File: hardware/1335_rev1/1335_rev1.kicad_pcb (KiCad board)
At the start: 2 copper layers, 45 x 45 mm, 11 parts, among them J1 Screw_Terminal_01x05, J2 Screw_Terminal_01x05, U1 A1335

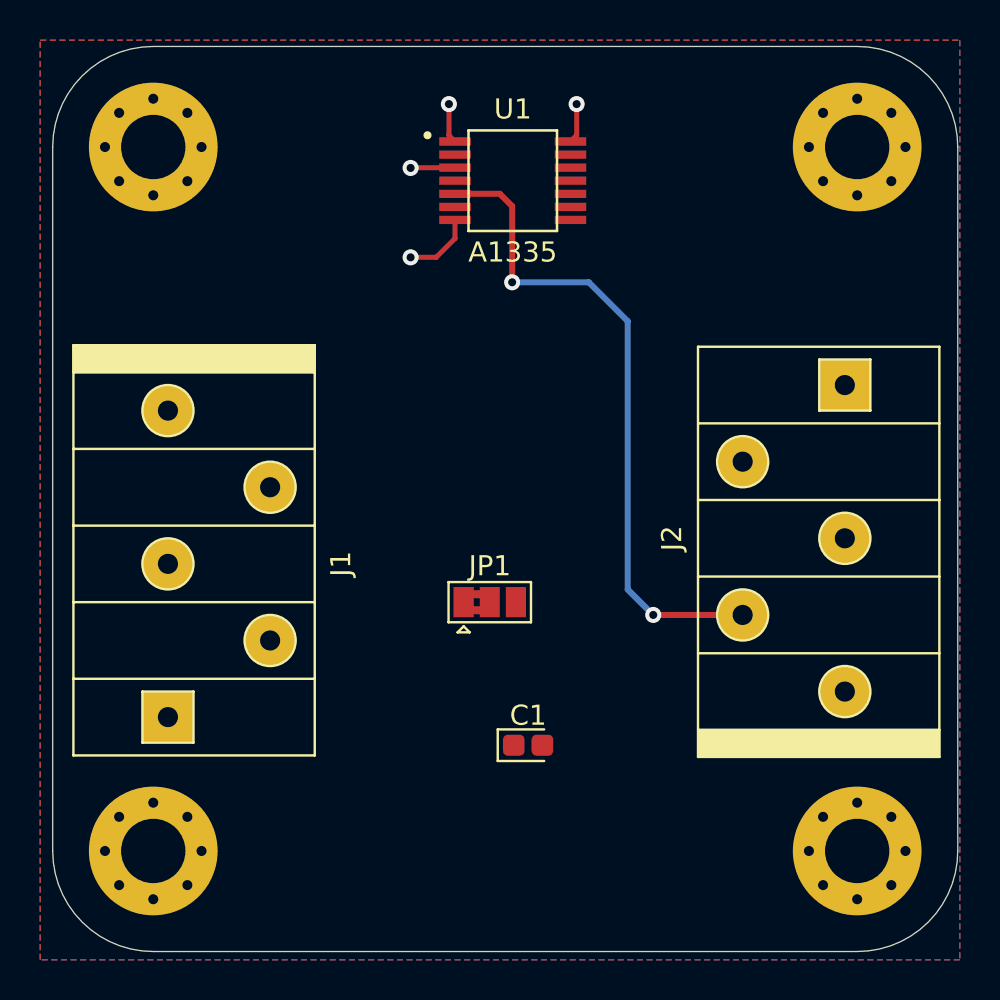
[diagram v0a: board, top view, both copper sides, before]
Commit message: Add 3d models, send to review pcb
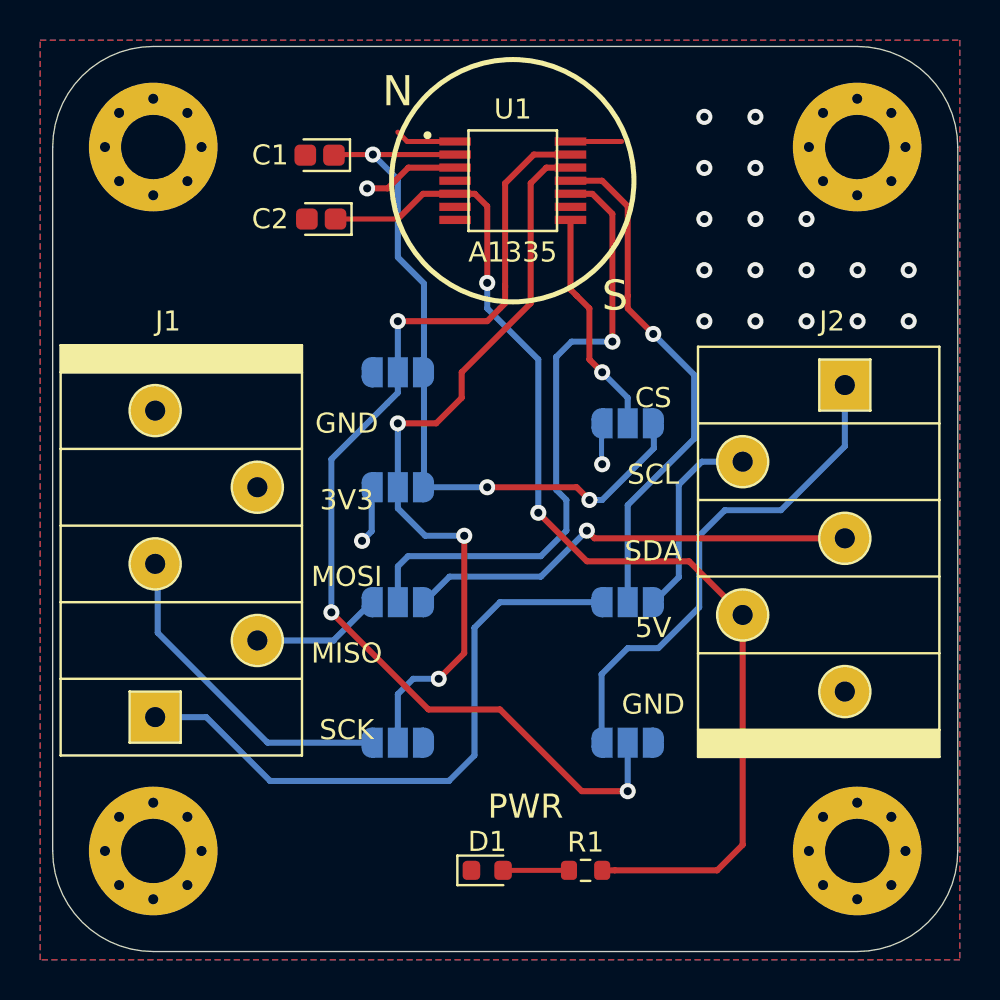
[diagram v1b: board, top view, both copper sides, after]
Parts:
- removed REF**: KiCad-Logo2_6mm_SilkScreen, Symbol:KiCad-Logo2_6mm_SilkScreen
- added C2: 100n, Capacitor_Tantalum_SMD:CP_EIA-1608-08_AVX-J, F.Cu at (133.3, 68.6)
- added D1: LED, LED_SMD:LED_0603_1608Metric, F.Cu at (141.6, 101.0)
- added JP2: Jumper_NC_Dual, Jumper:SolderJumper-3_P1.3mm_Open_RoundedPad1.0x1.5mm_NumberLabels, B.Cu at (148.6, 87.6)
- added JP3: Jumper_NC_Dual, Jumper:SolderJumper-3_P1.3mm_Open_RoundedPad1.0x1.5mm_NumberLabels, B.Cu at (148.6, 94.6)
- added JP4: Jumper_NC_Dual, Jumper:SolderJumper-3_P1.3mm_Open_RoundedPad1.0x1.5mm_NumberLabels, B.Cu at (137.2, 76.2)
- added JP5: Jumper_NC_Dual, Jumper:SolderJumper-3_P1.3mm_Open_RoundedPad1.0x1.5mm_NumberLabels, B.Cu at (137.2, 87.6)
- added JP6: Jumper_NC_Dual, Jumper:SolderJumper-3_P1.3mm_Open_RoundedPad1.0x1.5mm_NumberLabels, B.Cu at (137.2, 94.6)
- added JP7: Jumper_NC_Dual, Jumper:SolderJumper-3_P1.3mm_Open_RoundedPad1.0x1.5mm_NumberLabels, B.Cu at (137.2, 81.9)
- added R1: 1k, Resistor_SMD:R_0603_1608Metric, F.Cu at (146.5, 101.0)
- C1: value CP1 -> 100n
- JP1: value Jumper_3_Bridged12 -> Jumper_NC_Dual; footprint Jumper:SolderJumper-3_P1.3mm_Bridged2Bar12_Pad1.0x1.5mm -> Jumper:SolderJumper-3_P1.3mm_Open_RoundedPad1.0x1.5mm_NumberLabels; moved to B.Cu
- moved C1 31.1 mm to (133.3, 65.4), turned to 180 degrees
- moved JP1 11.2 mm to (148.6, 78.7), turned to 180 degrees
- moved G*** 1.27 mm to (142.2, 101.6)
- moved J1 0.64 mm to (125.1, 85.7)
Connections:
- JP1 pad 1: GND -> /BYP
- JP1 pad 3: /BYP -> GND
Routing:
- net /SA0-CS: track 0.00 -> 52.3 mm, vias 0 -> 3
- net /SA1-MOSI: track 0.00 -> 38.6 mm, vias 0 -> 3
- net /BYP: track 0.00 -> 37.6 mm, vias 0 -> 3
- net /SDA-MISO: track 0.00 -> 31.7 mm, vias 0 -> 1
- net SCK: track 0.00 -> 30.9 mm
- net /SCL-CLK: track 0.00 -> 25.8 mm, vias 0 -> 1
- net CS: track 0.00 -> 25.3 mm
- net +5V: track 33.0 -> 55.8 mm
- net SDA: track 0.00 -> 22.6 mm, vias 0 -> 1
- net MOSI: track 0.00 -> 16.4 mm
- net /ISEL: track 0.00 -> 11.3 mm, vias 0 -> 1
- net SCL: track 0.00 -> 10.0 mm
- net MISO: track 0.00 -> 6.49 mm
- net GND: track 9.71 -> 15.3 mm, vias 4 -> 20
- net Net-(D1-Pad2): track 0.00 -> 3.28 mm
- added copper zone on F.Cu, net GND
- removed copper zone on F.Cu, net (none)
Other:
- board text added: "3V3"
- board text added: "5V"
- board text added: "CS"
- board text added: "GND"
- board text added: "MISO"
- board text added: "MOSI"
- board text added: "N"
- board text added: "PWR"
- board text added: "S"
- board text added: "SCK"
- board text added: "SCL"
- board text added: "SDA"

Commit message: Add connectors and pull up resistors
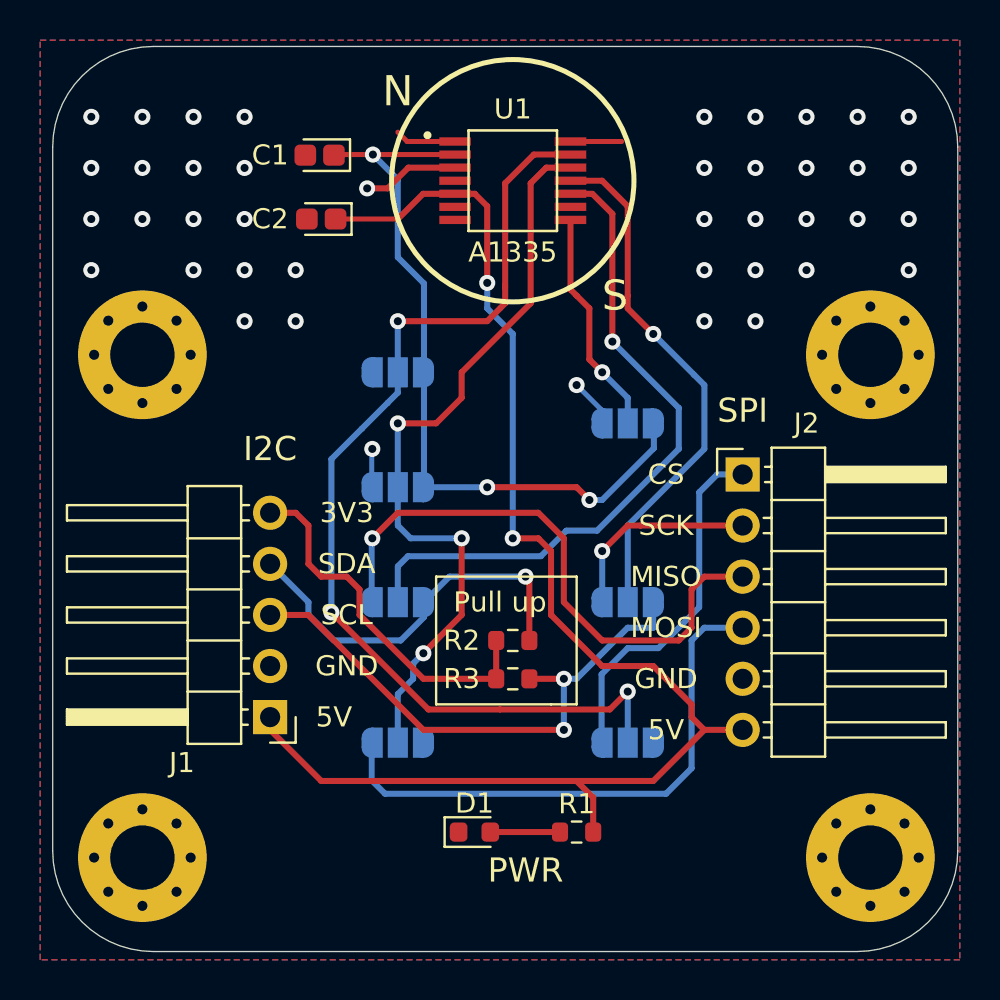
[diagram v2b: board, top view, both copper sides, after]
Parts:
- added R2: 1k, Resistor_SMD:R_0603_1608Metric, F.Cu at (142.9, 89.5)
- added R3: 1k, Resistor_SMD:R_0603_1608Metric, F.Cu at (142.9, 91.4)
- J1: footprint Terminal_Block_WR_TBL:terminal_block_1x05_45DEG_3.81MM_5POS -> Connector_PinHeader_2.54mm:PinHeader_1x05_P2.54mm_Horizontal
- J2: value Screw_Terminal_01x05 -> Screw_Terminal_01x06; footprint Terminal_Block_WR_TBL:terminal_block_1x05_45DEG_3.81MM_5POS -> Connector_PinHeader_2.54mm:PinHeader_1x06_P2.54mm_Horizontal
- moved H2 10.4 mm to (160.7, 75.3)
- moved H1 10.3 mm to (124.5, 75.3)
- moved J1 9.53 mm to (130.8, 93.3), turned to 180 degrees
- moved J2 5.99 mm to (154.3, 81.3), turned to 0 degrees
- moved D1 2.01 mm to (141.0, 99.1)
- moved R1 1.96 mm to (146.1, 99.1)
- moved H4 0.73 mm to (160.7, 100.3)
- moved H3 0.63 mm to (124.5, 100.3)
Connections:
- J1 pad 1: SCK -> +5V
- J1 pad 2: MISO -> GND
- J1 pad 3: MOSI -> SCL
- J1 pad 4: +3V3 -> SDA
- J1 pad 5: GND -> +3V3
- J2 pad 2: SCL -> SCK
- J2 pad 3: SDA -> MISO
- J2 pad 4: +5V -> MOSI
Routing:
- net MISO: track 6.49 -> 29.0 mm, vias 0 -> 1
- net SCK: track 30.9 -> 10.1 mm, vias 0 -> 1
- net +3V3: track 0.00 -> 18.4 mm
- net SCL: track 10.0 -> 28.0 mm, vias 0 -> 2
- net +5V: track 55.8 -> 70.2 mm
- net MOSI: track 16.4 -> 27.7 mm
- net CS: track 25.3 -> 17.9 mm
- net SDA: track 22.6 -> 19.7 mm
- net /SDA-MISO: track 31.7 -> 33.7 mm
- net /SA0-CS: track 52.3 -> 51.1 mm
- net GND: track 15.3 -> 14.7 mm, vias 20 -> 42
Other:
- board text added: "I2C"
- board text added: "Pull up"
- board text added: "SPI"

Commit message: Add F.sliks anotations
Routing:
- net GND: vias 42 -> 62
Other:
- board text added: "I2C Mode: jump pads 2-3"
- board text added: "SPI Mode: Jump pads 1-2"

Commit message: Updates
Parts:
- moved R1 2.01 mm to (145.4, 97.2)
- moved D1 2.01 mm to (140.3, 97.2)
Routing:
- net GND: track 14.7 -> 27.7 mm, vias 62 -> 66
- net +5V: track 70.2 -> 67.7 mm

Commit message: Updates in pcb
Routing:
- net GND: track 27.7 -> 28.4 mm
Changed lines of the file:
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@@
     (0 F.Cu signal)
     (31 B.Cu signal)
-    (32 B.Adhes user)
-    (33 F.Adhes user)
+    (32 B.Adhes user hide)
+    (33 F.Adhes user hide)
     (34 B.Paste user)
     (35 F.Paste user)
@@
     (38 B.Mask user)
     (39 F.Mask user)
-    (40 Dwgs.User user)
-    (41 Cmts.User user)
-    (42 Eco1.User user)
-    (43 Eco2.User user)
+    (40 Dwgs.User user hide)
+    (41 Cmts.User user hide)
+    (42 Eco1.User user hide)
+    (43 Eco2.User user hide)
     (44 Edge.Cuts user)
-    (45 Margin user)
-    (46 B.CrtYd user)
-    (47 F.CrtYd user)
+    (45 Margin user hide)
+    (46 B.CrtYd user hide)
+    (47 F.CrtYd user hide)
     (48 B.Fab user hide)
     (49 F.Fab user hide)
@@
       (outputformat 1)
       (mirror false)
-      (drillshape 1)
+      (drillshape 0)
       (scaleselection 1)
-      (outputdirectory ""))
+      (outputdirectory "../gerbers/"))
   )
   (net 0 "")
@@
       (effects (font (size 0.4 0.4) (thickness 0.06)))
     )
-    (pad 2 smd roundrect (at 0.7125 0 180) (size 1.075 1.05) (layers F.Cu F.Paste F.Mask) (roundrect_rratio 0.238095)
+    (pad 2 smd roundrect (at 0.7125 0 180) (size 1.075 1.05) (layers F.Cu F.Paste F.Mask) (roundrect_rratio 0.2380942857142857)
       (net 2 GND))
-    (pad 1 smd roundrect (at -0.7125 0 180) (size 1.075 1.05) (layers F.Cu F.Paste F.Mask) (roundrect_rratio 0.238095)
+    (pad 1 smd roundrect (at -0.7125 0 180) (size 1.075 1.05) (layers F.Cu F.Paste F.Mask) (roundrect_rratio 0.2380942857142857)
       (net 7 +5V))
     (model ${KISYS3DMOD}/Capacitor_Tantalum_SMD.3dshapes/CP_EIA-1608-08_AVX-J.wrl
@@
       (effects (font (size 0.4 0.4) (thickness 0.06)))
     )
-    (pad 1 smd roundrect (at -0.7125 0 180) (size 1.075 1.05) (layers F.Cu F.Paste F.Mask) (roundrect_rratio 0.238095)
+    (pad 1 smd roundrect (at -0.7125 0 180) (size 1.075 1.05) (layers F.Cu F.Paste F.Mask) (roundrect_rratio 0.2380942857142857)
       (net 1 /BYP))
-    (pad 2 smd roundrect (at 0.7125 0 180) (size 1.075 1.05) (layers F.Cu F.Paste F.Mask) (roundrect_rratio 0.238095)
+    (pad 2 smd roundrect (at 0.7125 0 180) (size 1.075 1.05) (layers F.Cu F.Paste F.Mask) (roundrect_rratio 0.2380942857142857)
       (net 2 GND))
     (model ${KISYS3DMOD}/Capacitor_Tantalum_SMD.3dshapes/CP_EIA-1608-08_AVX-J.wrl
@@
   (segment (start 136.652 67.056) (end 137.683 66.025) (width 0.3) (layer F.Cu) (net 2))
   (segment (start 145.745 64.725) (end 148.291 64.725) (width 0.25) (layer F.Cu) (net 2))
-  (via (at 146.05 76.835) (size 0.8) (drill 0.4) (layers F.Cu B.Cu) (net 2))
-  (segment (start 147.29 78.075) (end 146.05 76.835) (width 0.25) (layer B.Cu) (net 2))
+  (via (at 144.78 78.74) (size 0.8) (drill 0.4) (layers F.Cu B.Cu) (net 2))
   (segment (start 147.29 78.74) (end 147.29 78.075) (width 0.25) (layer B.Cu) (net 2))
   (via (at 135.89 80.01) (size 0.8) (drill 0.4) (layers F.Cu B.Cu) (net 2))
@@
   (segment (start 138.385 68.625) (end 137.795 69.215) (width 0.3) (layer F.Cu) (net 2))
   (segment (start 137.795 69.215) (end 137.795 69.85) (width 0.3) (layer F.Cu) (net 2))
+  (segment (start 147.29 78.74) (end 144.78 78.74) (width 0.3) (layer B.Cu) (net 2))
   (segment (start 154.305 83.82) (end 149.225 83.82) (width 0.3) (layer F.Cu) (net 3))
   (via (at 147.32 85.09) (size 0.8) (drill 0.4) (layers F.Cu B.Cu) (net 3))

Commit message: Send to review
Esteban Osella aprueba el diseño del PCB
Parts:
- moved C1 4.09 mm to (137.2, 64.1), turned to 90 degrees
- moved C2 3.86 mm to (137.2, 67.9), turned to 270 degrees
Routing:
- net GND: track 28.4 -> 23.6 mm
- net +5V: track 67.7 -> 64.1 mm
- net /BYP: track 37.6 -> 36.1 mm
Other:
- board text added: "Rev 2.0"

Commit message: Updates in pcb
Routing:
- net MOSI: track 27.7 -> 37.5 mm
- net /SA1-MOSI: track 38.1 -> 38.8 mm
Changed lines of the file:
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@@
     (thickness 1.6)
     (drawings 58)
-    (tracks 271)
+    (tracks 281)
     (zones 0)
     (modules 21)
@@
     (user_trace_width 0.3)
     (trace_clearance 0.2)
-    (zone_clearance 0.508)
+    (zone_clearance 3)
     (zone_45_only no)
     (trace_min 0.2)
@@
   (segment (start 151.765 89.535) (end 152.4 88.9) (width 0.3) (layer B.Cu) (net 5))
   (segment (start 151.765 95.885) (end 151.765 89.535) (width 0.3) (layer B.Cu) (net 5))
-  (segment (start 150.495 97.155) (end 151.765 95.885) (width 0.3) (layer B.Cu) (net 5))
-  (segment (start 136.525 97.155) (end 150.495 97.155) (width 0.3) (layer B.Cu) (net 5))
-  (segment (start 135.86 96.49) (end 136.525 97.155) (width 0.3) (layer B.Cu) (net 5))
-  (segment (start 135.86 94.615) (end 135.86 96.49) (width 0.3) (layer B.Cu) (net 5))
+  (segment (start 151.13 96.52) (end 151.765 95.885) (width 0.3) (layer B.Cu) (net 5))
+  (segment (start 135.86 92.105) (end 137.795 90.17) (width 0.3) (layer B.Cu) (net 5))
+  (segment (start 139.31001 88.65499) (end 140.335 87.63) (width 0.3) (layer B.Cu) (net 5))
+  (segment (start 144.145 94.615) (end 144.78 95.25) (width 0.3) (layer B.Cu) (net 5))
+  (segment (start 137.795 90.17) (end 138.43 90.17) (width 0.3) (layer B.Cu) (net 5))
+  (segment (start 135.86 94.615) (end 135.86 92.105) (width 0.3) (layer B.Cu) (net 5))
+  (segment (start 144.78 95.25) (end 146.05 95.25) (width 0.3) (layer B.Cu) (net 5))
+  (segment (start 146.05 95.25) (end 147.32 96.52) (width 0.3) (layer B.Cu) (net 5))
+  (segment (start 138.43 90.17) (end 139.31001 89.28999) (width 0.3) (layer B.Cu) (net 5))
+  (segment (start 147.32 96.52) (end 151.13 96.52) (width 0.3) (layer B.Cu) (net 5))
+  (segment (start 140.335 87.63) (end 143.51 87.63) (width 0.3) (layer B.Cu) (net 5))
+  (segment (start 139.31001 89.28999) (end 139.31001 88.65499) (width 0.3) (layer B.Cu) (net 5))
+  (segment (start 143.51 87.63) (end 144.145 88.265) (width 0.3) (layer B.Cu) (net 5))
+  (segment (start 144.145 88.265) (end 144.145 94.615) (width 0.3) (layer B.Cu) (net 5))
   (segment (start 142.05 89.535) (end 142.05 91.44) (width 0.3) (layer F.Cu) (net 6))
   (segment (start 138.43 91.44) (end 142.05 91.44) (width 0.3) (layer F.Cu) (net 6))
@@
   (via (at 140.335 84.455) (size 0.8) (drill 0.4) (layers F.Cu B.Cu) (net 17))
   (segment (start 137.795 84.455) (end 140.335 84.455) (width 0.3) (layer B.Cu) (net 17))
-  (segment (start 140.335 84.455) (end 140.335 87.63) (width 0.3) (layer F.Cu) (net 17))
-  (segment (start 140.335 87.63) (end 140.335 88.265) (width 0.3) (layer F.Cu) (net 17))
-  (via (at 138.43 90.17) (size 0.8) (drill 0.4) (layers F.Cu B.Cu) (net 17))
-  (segment (start 140.335 88.265) (end 138.43 90.17) (width 0.3) (layer F.Cu) (net 17))
-  (segment (start 137.922 90.678) (end 137.922 91.44) (width 0.3) (layer B.Cu) (net 17))
-  (segment (start 138.43 90.17) (end 137.922 90.678) (width 0.3) (layer B.Cu) (net 17))
+  (segment (start 137.922 91.44) (end 139.065 91.44) (width 0.3) (layer B.Cu) (net 17))
+  (segment (start 139.065 91.44) (end 140.335 90.17) (width 0.3) (layer B.Cu) (net 17))
+  (via (at 140.335 88.9) (size 0.8) (drill 0.4) (layers F.Cu B.Cu) (net 17))
+  (segment (start 140.335 90.17) (end 140.335 88.9) (width 0.3) (layer B.Cu) (net 17))
+  (segment (start 140.335 87.63) (end 140.335 84.455) (width 0.3) (layer F.Cu) (net 17))
+  (segment (start 140.335 88.9) (end 140.335 87.63) (width 0.3) (layer F.Cu) (net 17))
   (segment (start 145.745 65.375) (end 143.921 65.375) (width 0.3) (layer F.Cu) (net 18))
   (segment (start 143.921 65.375) (end 142.494 66.802) (width 0.3) (layer F.Cu) (net 18))
